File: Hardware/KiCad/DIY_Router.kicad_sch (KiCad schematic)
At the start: 28 parts, among them IC1 HLK-7628N, IC2 TPS62A06ADRLR, J1 2171790001, J5 Conn_01x06_Pin, J6 Conn_02x07_Odd_Even, SW1 436333033816, SW2 436333033816, U2 USBLC6-2SC6Y

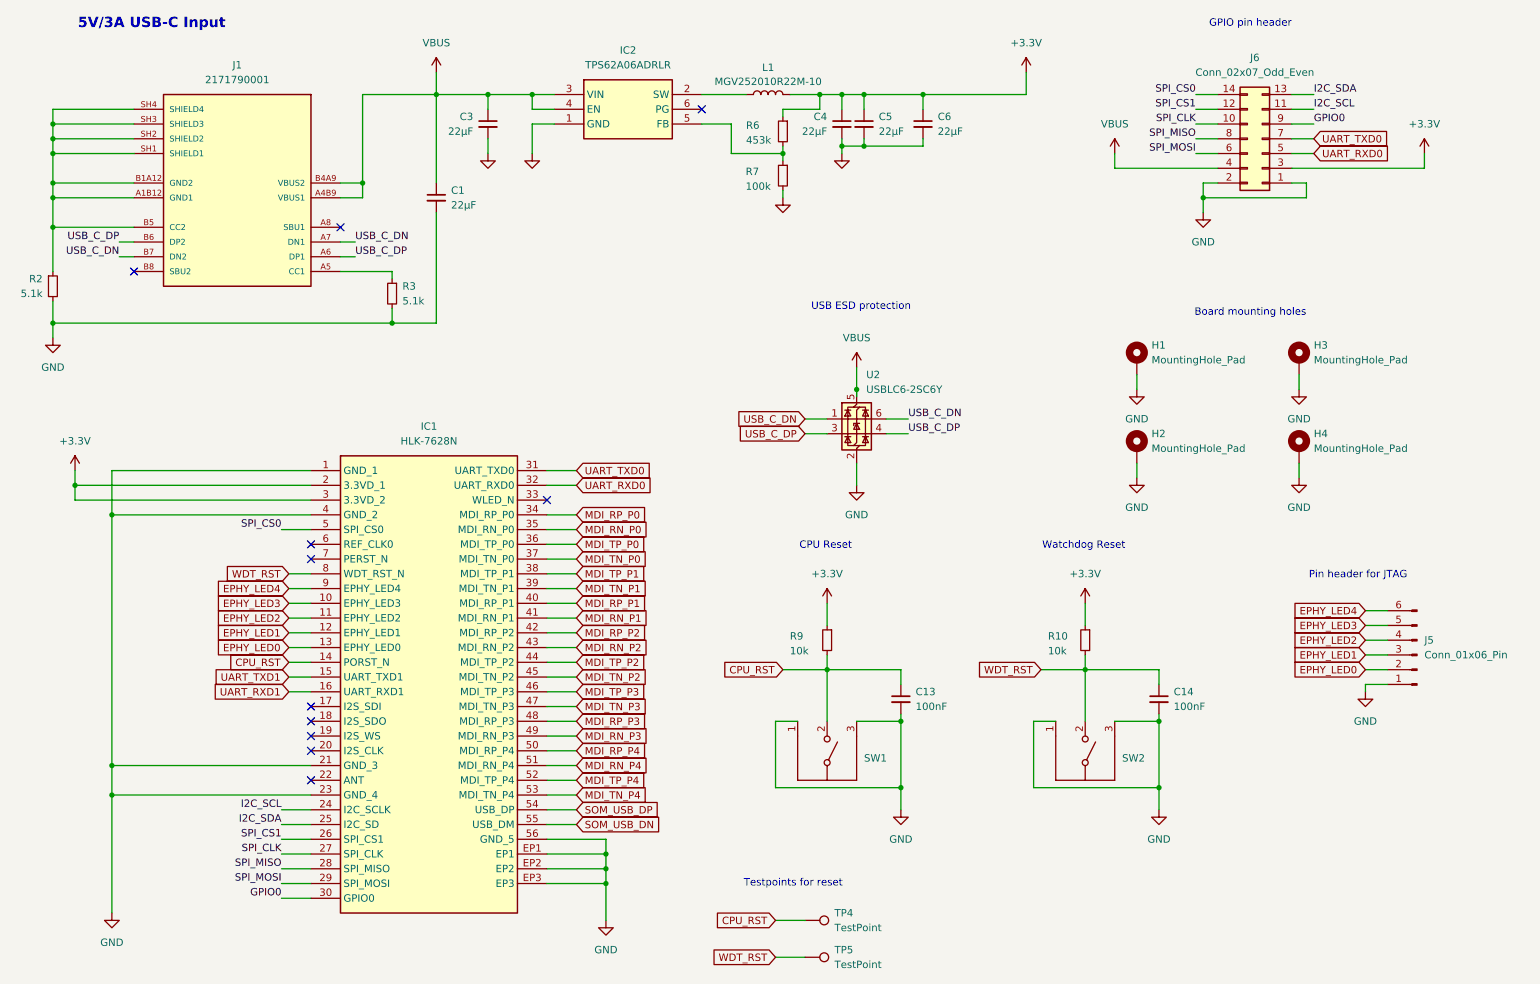
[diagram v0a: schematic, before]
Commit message: Rename all MDI signals to match kicad diffpair naming scheme
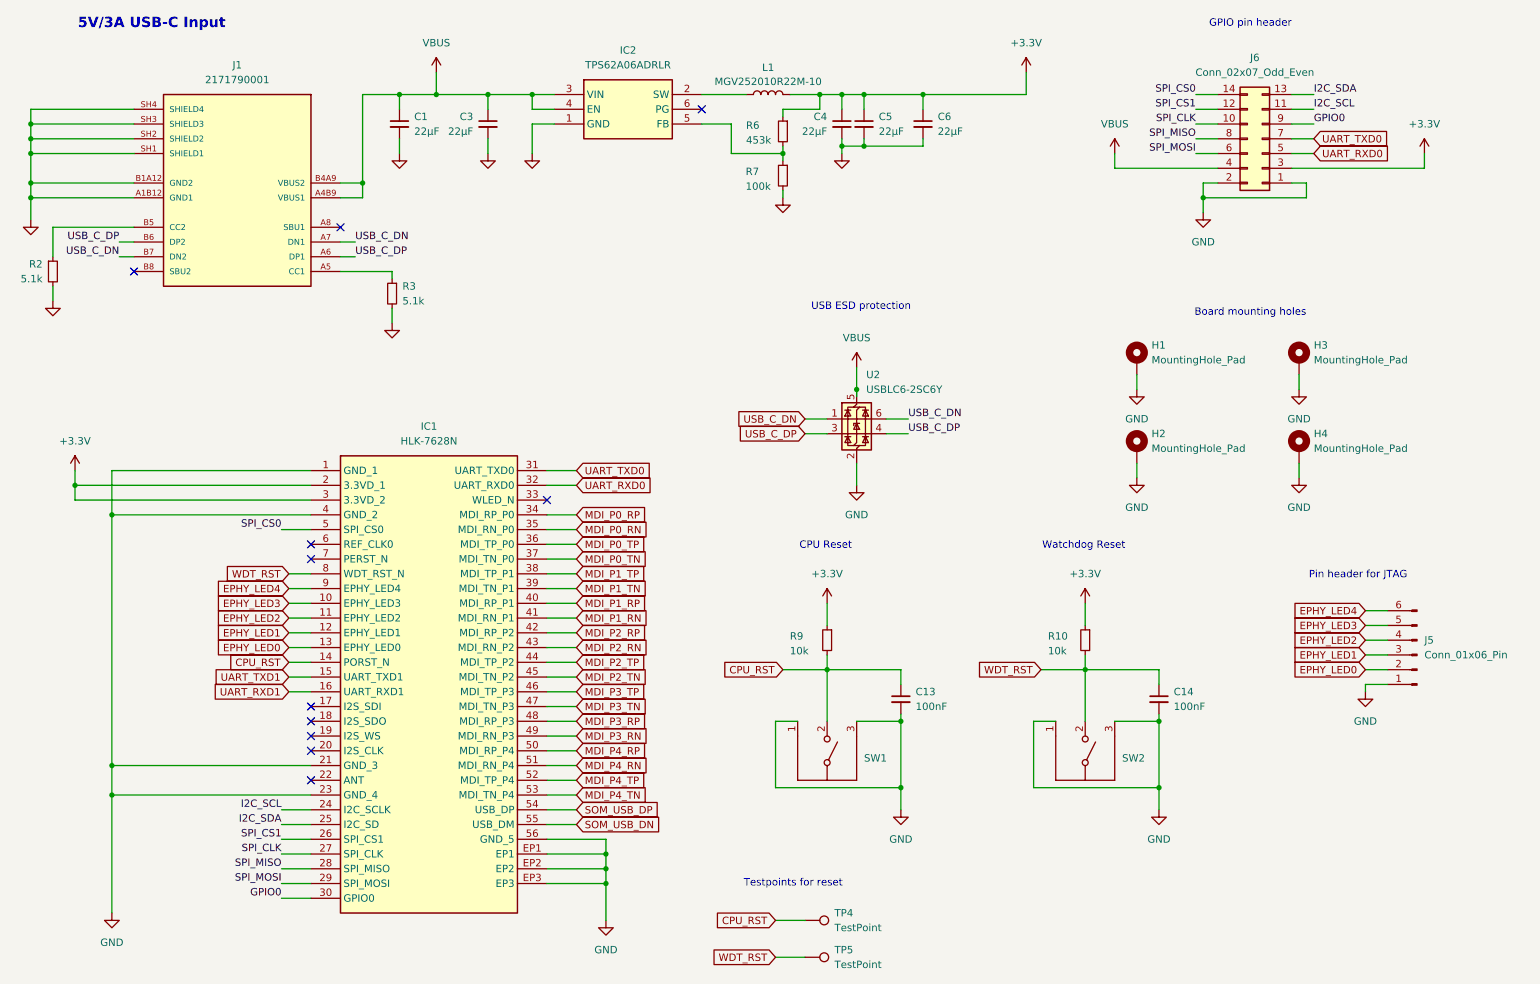
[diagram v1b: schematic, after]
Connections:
- net GND: now also J1.A1B12 (GND1), J1.B1A12 (GND2), J1.SH1 (SHIELD1), J1.SH2 (SHIELD2), J1.SH3 (SHIELD3), J1.SH4 (SHIELD4)
- net MDI_RN_P0 renamed MDI_P0_RN
- net MDI_RN_P1 renamed MDI_P1_RN
- net MDI_RN_P2 renamed MDI_P2_RN
- net MDI_RN_P3 renamed MDI_P3_RN
- net MDI_RN_P4 renamed MDI_P4_RN
- net MDI_RP_P0 renamed MDI_P0_RP
- net MDI_RP_P1 renamed MDI_P1_RP
- net MDI_RP_P2 renamed MDI_P2_RP
- net MDI_RP_P3 renamed MDI_P3_RP
- net MDI_RP_P4 renamed MDI_P4_RP
- net MDI_TN_P0 renamed MDI_P0_TN
- net MDI_TN_P1 renamed MDI_P1_TN
- net MDI_TN_P2 renamed MDI_P2_TN
- net MDI_TN_P3 renamed MDI_P3_TN
- net MDI_TN_P4 renamed MDI_P4_TN
- net MDI_TP_P0 renamed MDI_P0_TP
- net MDI_TP_P1 renamed MDI_P1_TP
- net MDI_TP_P2 renamed MDI_P2_TP
- net MDI_TP_P3 renamed MDI_P3_TP
- net MDI_TP_P4 renamed MDI_P4_TP
- new net: J1.B5 (CC2), R2.1
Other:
- moved on the sheet: C1

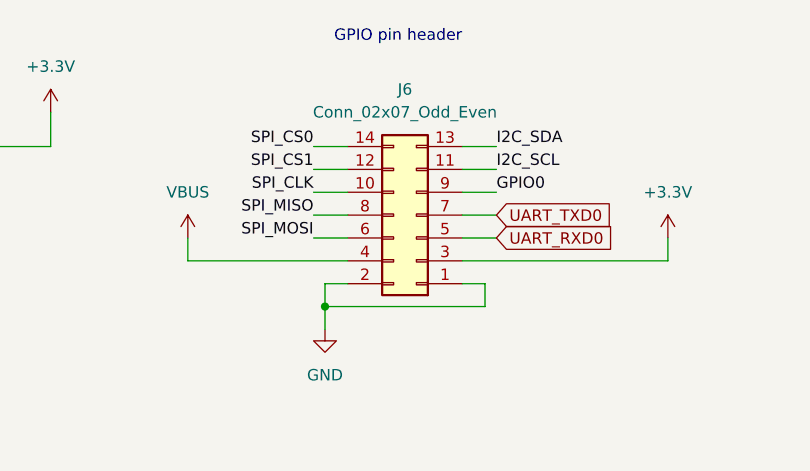
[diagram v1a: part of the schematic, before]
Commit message: Hardware: Lay out and route GPIO Header, USB and some other stuff
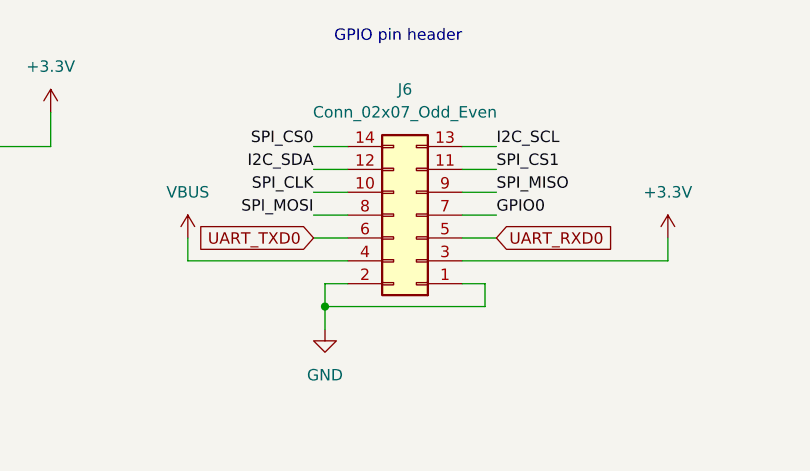
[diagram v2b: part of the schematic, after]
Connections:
- net GPIO0: now also J6.7 (Pin_7); no longer J6.9 (Pin_9)
- net I2C_SCL: now also J6.13 (Pin_13); no longer J6.11 (Pin_11)
- net I2C_SDA: now also J6.12 (Pin_12); no longer J6.13 (Pin_13)
- net SPI_CS1: now also J6.11 (Pin_11); no longer J6.12 (Pin_12)
- net SPI_MISO: now also J6.9 (Pin_9); no longer J6.8 (Pin_8)
- net SPI_MOSI: now also J6.8 (Pin_8); no longer J6.6 (Pin_6)
- net UART_TXD0: now also J6.6 (Pin_6); no longer J6.7 (Pin_7)
